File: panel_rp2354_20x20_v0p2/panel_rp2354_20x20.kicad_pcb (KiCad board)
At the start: 6 copper layers, 45.4 x 45.4 mm, 557 parts, among them J1 Conn_01x04, J2 Conn_01x05, J3 Conn_01x05, J4 Conn_01x05, J5 Conn_01x05, SW1 SW_Push, SW2 SW_Push, U1 APS6404L-3SQR, U10 UCC27517, U11 UCC27517, U12 UCC27517, U13 UCC27517, U14 UCC27517, U15 UCC27517, U16 UCC27517, U17 UCC27517, U18 UCC27517, U19 UCC27517, U2 RP2354B_80QFN, U20 UCC27517, U21 UCC27517, U22 UCC27517, U23 UCC27517, U24 UCC27517, U25 UCC27517, U26 UCC27517, U27 UCC27517, U28 UCC27517, U29 UCC27517, U3 UCC27517, U30 UCC27517, U31 UCC27517, U32 UCC27517, U33 UCC27517, U34 UCC27517, U35 UCC27517, U36 UCC27517, U37 UCC27517, U38 UCC27517, U39 UCC27517, U4 UCC27517, U40 UCC27517, U41 UCC27517, U42 UCC27517, U43 AP2112K-3.3, U5 UCC27517, U6 UCC27517, U7 UCC27517, U8 UCC27517, U9 UCC27517, Y1 ABM8-272-T3

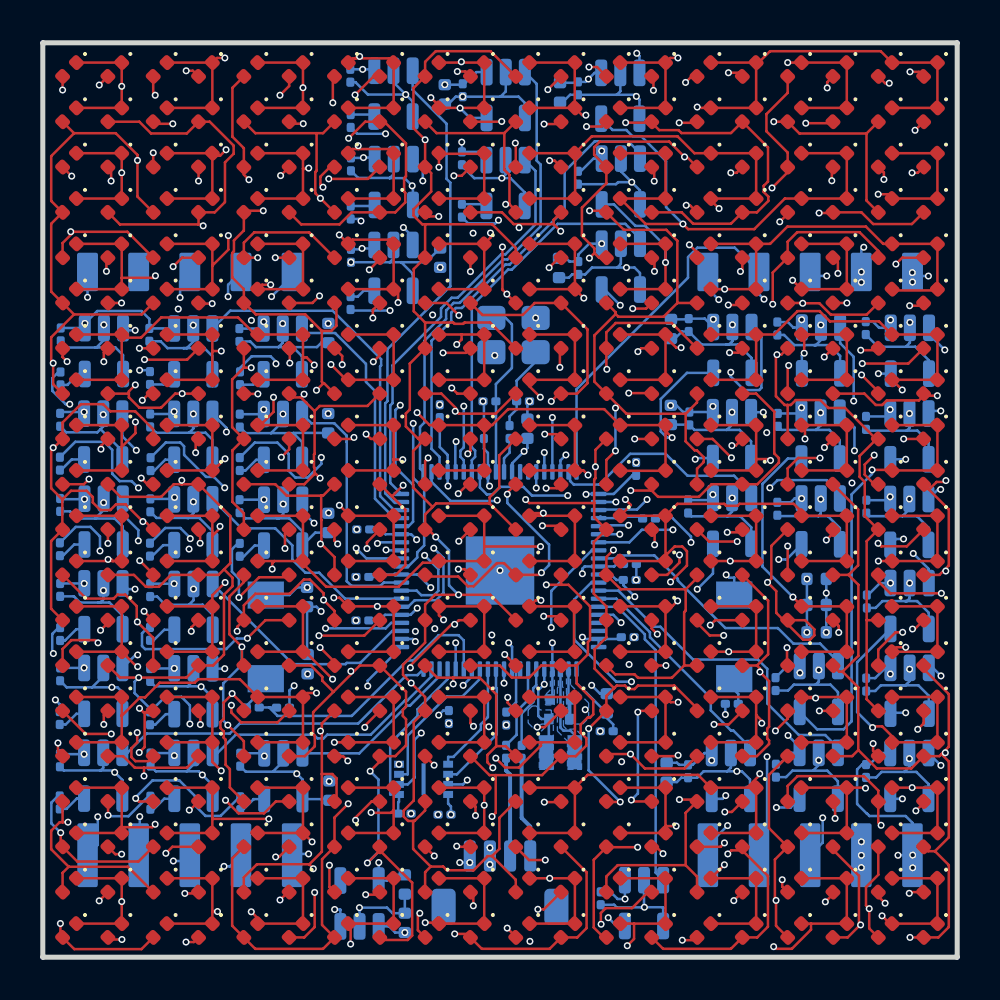
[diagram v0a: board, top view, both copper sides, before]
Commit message: shrink to 45x45
- a few more vias, moved 2 capacitors by <1mm
- moved text to silkscreen
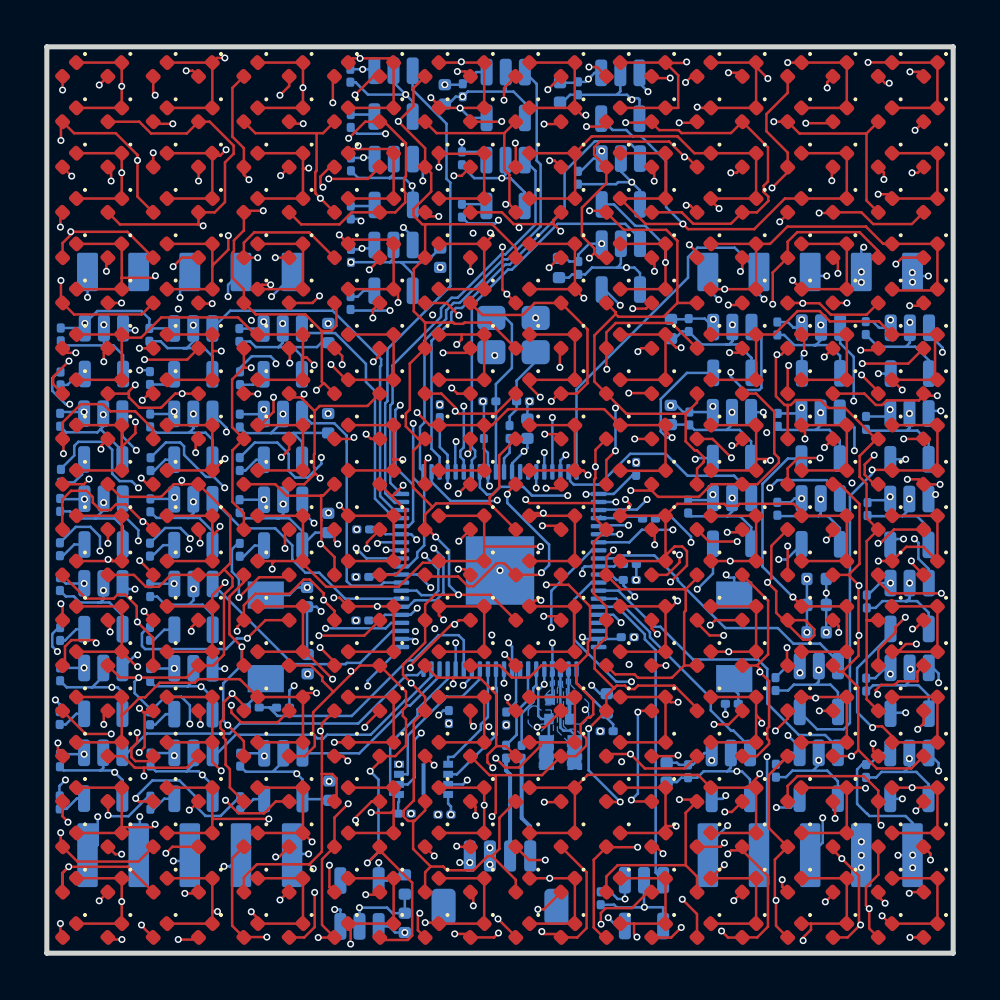
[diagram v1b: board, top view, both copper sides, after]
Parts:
- moved R21 0.61 mm to (50.7, 71.3)
- moved C25 0.29 mm to (50.6, 76.7)
- moved C52 0.13 mm to (90.8, 73.0)
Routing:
- net Net-(D1-A): track 105.2 -> 110.9 mm, vias 15 -> 17
- net Net-(D381-A): track 125.7 -> 120.2 mm, vias 12 -> 18
- net Net-(D41-A): track 119.3 -> 114.5 mm, vias 13 -> 18
- net /drivers/ROW_14: track 81.1 -> 83.0 mm
- net Net-(D361-A): track 150.6 -> 152.0 mm
- net /drivers/ROW_09: track 93.9 -> 92.7 mm, vias 7 -> 6
- net /drivers/ROW_MCU_12: track 17.9 -> 19.0 mm
- net Net-(D161-A): track 114.2 -> 113.2 mm, vias 7 -> 8
- net /drivers/ROW_00: track 69.6 -> 70.6 mm
- net Net-(D341-A): track 143.8 -> 142.9 mm
- net Net-(D261-A): track 143.3 -> 144.1 mm
- net /drivers/ROW_MCU_13: track 18.9 -> 18.2 mm
- net Net-(D241-A): track 139.4 -> 140.1 mm
- net Net-(D281-A): track 120.9 -> 120.3 mm
- net Net-(D121-A): track 109.8 -> 109.2 mm, vias 11 -> 13
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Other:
- board size 45.4 x 45.4 mm -> 45 x 45 mm
